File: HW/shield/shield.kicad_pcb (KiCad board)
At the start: 2 copper layers, 76.7 x 57 mm, 82 parts, among them J1 TRG, J2 E-STOP, J3 UART, J4 IO, J5 LDP-C BOB, J6 VIN, J7 BREAK, Q1 BSS138, Q2 BSS138, Q3 BSS138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

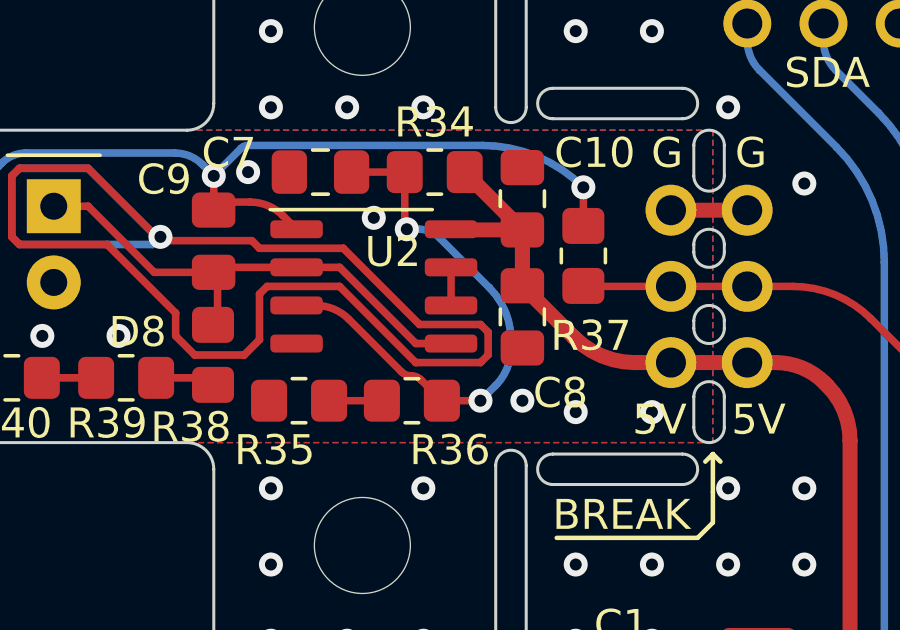
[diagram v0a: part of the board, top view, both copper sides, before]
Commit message: added readback on startup
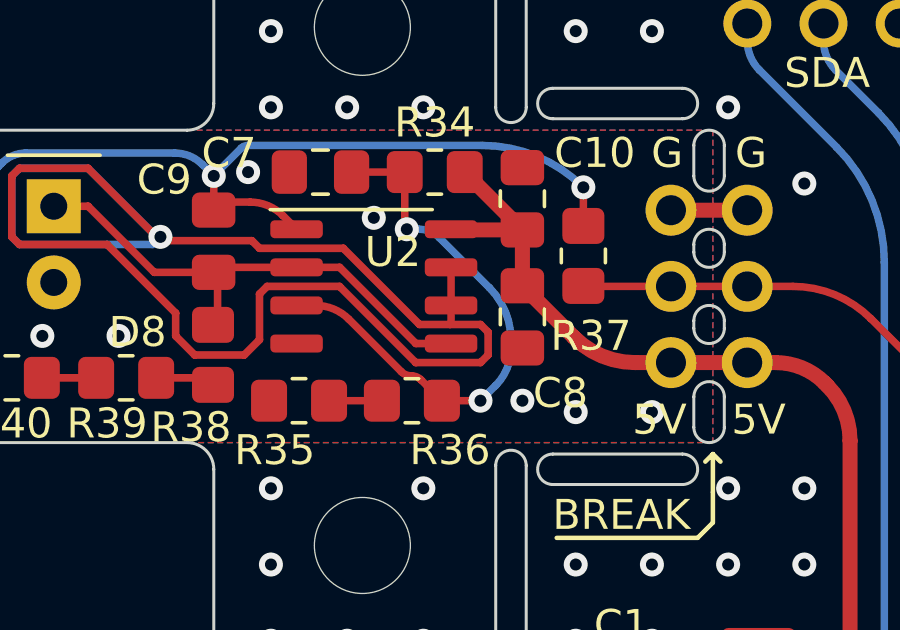
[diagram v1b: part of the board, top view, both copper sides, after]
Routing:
- net /GUARD: track 1.13 -> 57.0 mm, vias 0 -> 1
- net (no net): track 55.2 -> 0.00 mm, vias 1 -> 0
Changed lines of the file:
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@@
     (effects (font (size 1 1) (thickness 0.15)))
   )
-  (segment (start 129.667 85.852) (end 131.699 85.852) (width 0.254) (layer "F.Cu") (net 0))
-  (segment (start 116.332 83.185) (end 116.078 82.931) (width 0.254) (layer "F.Cu") (net 0))
-  (segment (start 129.54 87.122) (end 127 84.582) (width 0.254) (layer "F.Cu") (net 0))
-  (segment (start 131.699 85.852) (end 131.953 86.106) (width 0.254) (layer "F.Cu") (net 0))
-  (segment (start 118.618 80.645) (end 120.904 82.931) (width 0.254) (layer "F.Cu") (net 0))
-  (segment (start 124.333 84.836) (end 124.333 86.36) (width 0.254) (layer "F.Cu") (net 0))
-  (segment (start 122.17134 86.868) (end 121.539 86.23566) (width 0.254) (layer "F.Cu") (net 0))
-  (segment (start 121.031 82.931) (end 121.158 83.058) (width 0.254) (layer "F.Cu") (net 0))
-  (segment (start 116.078 82.931) (end 116.078 80.899) (width 0.254) (layer "F.Cu") (net 0))
-  (segment (start 116.332 80.645) (end 118.618 80.645) (width 0.254) (layer "F.Cu") (net 0))
-  (segment (start 121.539 85.471) (end 119.253 83.185) (width 0.254) (layer "F.Cu") (net 0))
-  (segment (start 119.253 83.185) (end 116.332 83.185) (width 0.254) (layer "F.Cu") (net 0))
-  (segment (start 124.333 83.312) (end 127.127 83.312) (width 0.254) (layer "F.Cu") (net 0))
-  (segment (start 121.158 83.058) (end 124.079 83.058) (width 0.254) (layer "F.Cu") (net 0))
-  (segment (start 116.078 80.899) (end 116.332 80.645) (width 0.254) (layer "F.Cu") (net 0))
-  (segment (start 120.904 82.931) (end 121.031 82.931) (width 0.254) (layer "F.Cu") (net 0))
-  (segment (start 131.953 86.106) (end 131.953 86.868) (width 0.254) (layer "F.Cu") (net 0))
-  (segment (start 121.539 86.23566) (end 121.539 85.471) (width 0.254) (layer "F.Cu") (net 0))
-  (segment (start 131.953 86.868) (end 131.699 87.122) (width 0.254) (layer "F.Cu") (net 0))
-  (segment (start 127 84.582) (end 124.587 84.582) (width 0.254) (layer "F.Cu") (net 0))
-  (segment (start 127.127 83.312) (end 129.667 85.852) (width 0.254) (layer "F.Cu") (net 0))
-  (segment (start 124.333 86.36) (end 123.825 86.868) (width 0.254) (layer "F.Cu") (net 0))
-  (segment (start 124.079 83.058) (end 124.333 83.312) (width 0.254) (layer "F.Cu") (net 0))
-  (segment (start 124.587 84.582) (end 124.333 84.836) (width 0.254) (layer "F.Cu") (net 0))
-  (segment (start 123.825 86.868) (end 122.17134 86.868) (width 0.254) (layer "F.Cu") (net 0))
-  (segment (start 131.699 87.122) (end 129.54 87.122) (width 0.254) (layer "F.Cu") (net 0))
-  (via (at 121.031 82.931) (size 0.8) (drill 0.4) (layers "F.Cu" "B.Cu") (net 0))
-  (segment (start 120.777 83.185) (end 116.332 83.185) (width 0.254) (layer "B.Cu") (net 0))
-  (segment (start 116.332 80.645) (end 118.618 80.645) (width 0.254) (layer "B.Cu") (net 0))
-  (segment (start 118.618 80.645) (end 120.904 82.931) (width 0.254) (layer "B.Cu") (net 0))
-  (segment (start 116.332 83.185) (end 116.078 82.931) (width 0.254) (layer "B.Cu") (net 0))
-  (segment (start 116.078 80.899) (end 116.332 80.645) (width 0.254) (layer "B.Cu") (net 0))
-  (segment (start 121.031 82.931) (end 120.777 83.185) (width 0.254) (layer "B.Cu") (net 0))
-  (segment (start 116.078 82.931) (end 116.078 80.899) (width 0.254) (layer "B.Cu") (net 0))
-  (segment (start 120.904 82.931) (end 121.031 82.931) (width 0.254) (layer "B.Cu") (net 0))
   (segment (start 173.101 113.157) (end 174.147078 114.203078) (width 0.254) (layer "F.Cu") (net 4))
   (segment (start 162.220644 116.409) (end 160.228 116.409) (width 0.254) (layer "F.Cu") (net 4))
@@
   (segment (start 156.854 88.138) (end 158.639 88.138) (width 0.25) (layer "F.Cu") (net 34))
   (segment (start 156.854 86.106) (end 158.639 86.106) (width 0.25) (layer "F.Cu") (net 35))
+  (segment (start 116.332 83.185) (end 116.078 82.931) (width 0.254) (layer "F.Cu") (net 36))
+  (segment (start 129.54 87.122) (end 127 84.582) (width 0.254) (layer "F.Cu") (net 36))
+  (segment (start 131.699 85.852) (end 131.953 86.106) (width 0.254) (layer "F.Cu") (net 36))
+  (segment (start 129.667 85.852) (end 130.683 85.852) (width 0.254) (layer "F.Cu") (net 36))
+  (segment (start 118.618 80.645) (end 120.904 82.931) (width 0.254) (layer "F.Cu") (net 36))
+  (segment (start 124.333 84.836) (end 124.333 86.36) (width 0.254) (layer "F.Cu") (net 36))
+  (segment (start 122.17134 86.868) (end 121.539 86.23566) (width 0.254) (layer "F.Cu") (net 36))
+  (segment (start 121.031 82.931) (end 121.158 83.058) (width 0.254) (layer "F.Cu") (net 36))
+  (segment (start 130.718 85.817) (end 130.683 85.852) (width 0.25) (layer "F.Cu") (net 36))
+  (segment (start 116.078 82.931) (end 116.078 80.899) (width 0.254) (layer "F.Cu") (net 36))
+  (segment (start 116.332 80.645) (end 118.618 80.645) (width 0.254) (layer "F.Cu") (net 36))
+  (segment (start 121.539 85.471) (end 119.253 83.185) (width 0.254) (layer "F.Cu") (net 36))
+  (segment (start 119.253 83.185) (end 116.332 83.185) (width 0.254) (layer "F.Cu") (net 36))
+  (segment (start 124.333 83.312) (end 127.127 83.312) (width 0.254) (layer "F.Cu") (net 36))
+  (segment (start 121.158 83.058) (end 124.079 83.058) (width 0.254) (layer "F.Cu") (net 36))
+  (segment (start 130.718 85.217) (end 130.718 85.817) (width 0.25) (layer "F.Cu") (net 36))
+  (segment (start 116.078 80.899) (end 116.332 80.645) (width 0.254) (layer "F.Cu") (net 36))
+  (segment (start 120.904 82.931) (end 121.031 82.931) (width 0.254) (layer "F.Cu") (net 36))
+  (segment (start 130.683 85.852) (end 131.699 85.852) (width 0.254) (layer "F.Cu") (net 36))
+  (segment (start 131.953 86.106) (end 131.953 86.868) (width 0.254) (layer "F.Cu") (net 36))
+  (segment (start 121.539 86.23566) (end 121.539 85.471) (width 0.254) (layer "F.Cu") (net 36))
+  (segment (start 131.953 86.868) (end 131.699 87.122) (width 0.254) (layer "F.Cu") (net 36))
+  (segment (start 127 84.582) (end 124.587 84.582) (width 0.254) (layer "F.Cu") (net 36))
+  (segment (start 127.127 83.312) (end 129.667 85.852) (width 0.254) (layer "F.Cu") (net 36))
+  (segment (start 124.333 86.36) (end 123.825 86.868) (width 0.254) (layer "F.Cu") (net 36))
+  (segment (start 124.079 83.058) (end 124.333 83.312) (width 0.254) (layer "F.Cu") (net 36))
   (segment (start 130.718 85.078624) (end 130.718 83.947) (width 0.25) (layer "F.Cu") (net 36))
+  (segment (start 124.587 84.582) (end 124.333 84.836) (width 0.254) (layer "F.Cu") (net 36))
+  (segment (start 123.825 86.868) (end 122.17134 86.868) (width 0.254) (layer "F.Cu") (net 36))
+  (segment (start 131.699 87.122) (end 129.54 87.122) (width 0.254) (layer "F.Cu") (net 36))
+  (via (at 121.031 82.931) (size 0.8) (drill 0.4) (layers "F.Cu" "B.Cu") (net 36))
+  (segment (start 120.777 83.185) (end 116.332 83.185) (width 0.254) (layer "B.Cu") (net 36))
+  (segment (start 116.332 80.645) (end 118.618 80.645) (width 0.254) (layer "B.Cu") (net 36))
+  (segment (start 118.618 80.645) (end 120.904 82.931) (width 0.254) (layer "B.Cu") (net 36))
+  (segment (start 116.332 83.185) (end 116.078 82.931) (width 0.254) (layer "B.Cu") (net 36))
+  (segment (start 116.078 80.899) (end 116.332 80.645) (width 0.254) (layer "B.Cu") (net 36))
+  (segment (start 121.031 82.931) (end 120.777 83.185) (width 0.254) (layer "B.Cu") (net 36))
+  (segment (start 116.078 82.931) (end 116.078 80.899) (width 0.254) (layer "B.Cu") (net 36))
+  (segment (start 120.904 82.931) (end 121.031 82.931) (width 0.254) (layer "B.Cu") (net 36))
   (segment (start 137.630075 111.980424) (end 137.159999 112.450499) (width 0.25) (layer "F.Cu") (net 37))
   (segment (start 128.9205 118.069) (end 128.26 118.069) (width 0.25) (layer "F.Cu") (net 37))
